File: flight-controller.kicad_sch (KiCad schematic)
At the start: 58 parts, among them J1 USB_C_Receptacle_USB2.0, Q1 NMOS, SW1 SW_Push, U1 AT32F435RGT7, U2 BMI270, U3 BMP280, U4 W25N01GVZEIG, U5 AT7456E, U6 TPS54302, U7 TPS54302, U8 TLV75733PDBV, U9 USBLC6-2P6

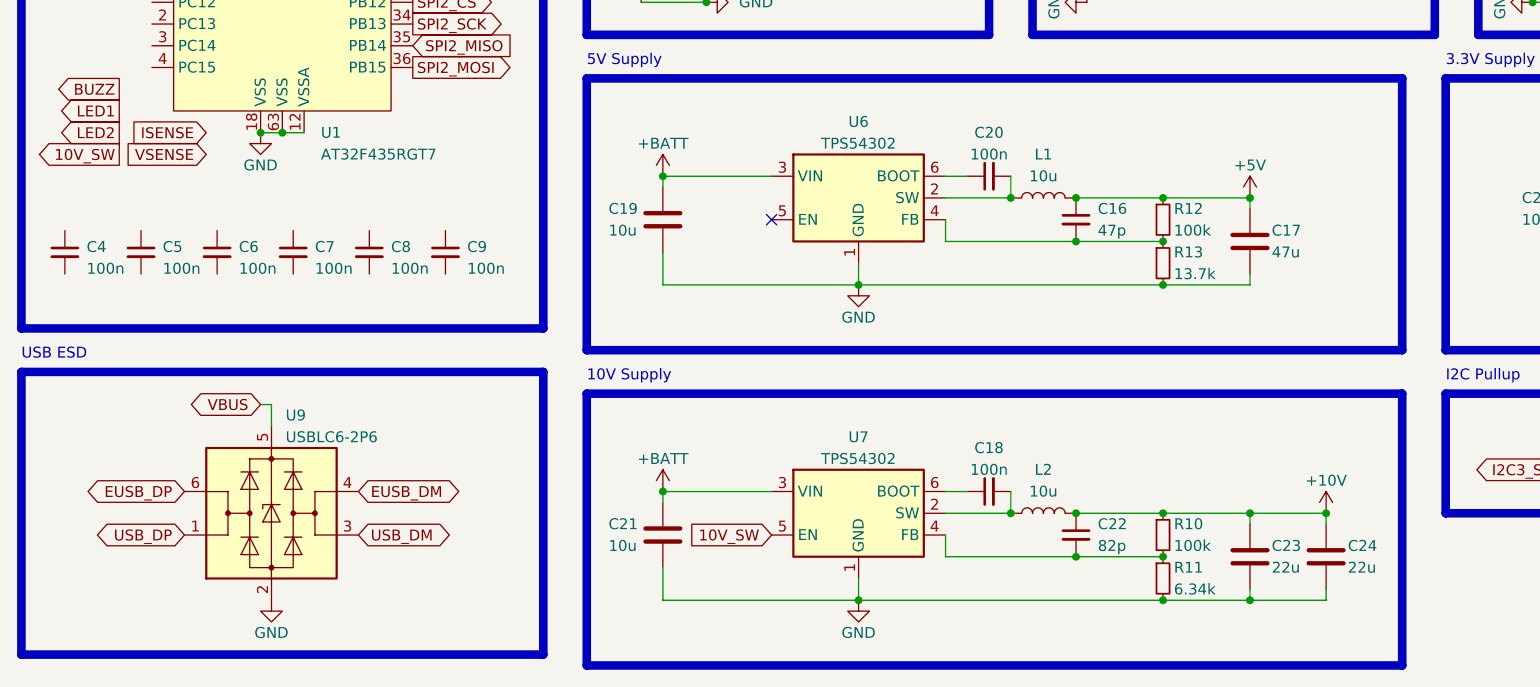
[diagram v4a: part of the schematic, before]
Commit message: Add LCSC part numbers for major parts. Provisionally delect power supply capacitors and inductors.
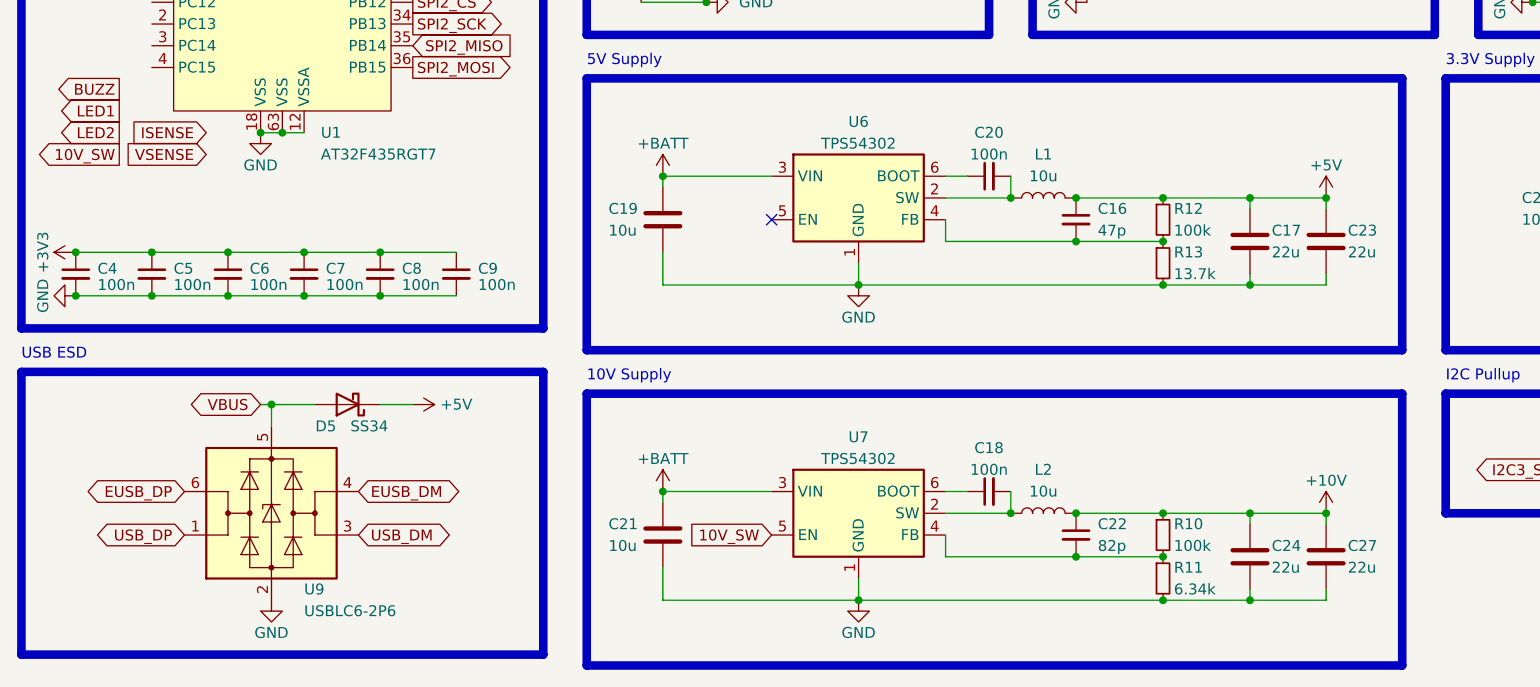
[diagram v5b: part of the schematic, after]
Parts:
- added C27: 22u, Capacitor_SMD:C_1206_3216Metric, symbol Device:C
- added D5: SS34, Diode_SMD:D_SMA, symbol Device:D_Schottky
- C17: value 47u -> 22u; footprint (none) -> Capacitor_SMD:C_1206_3216Metric; LCSC (none) -> C12891
- C23, C24: footprint (none) -> Capacitor_SMD:C_1206_3216Metric; LCSC (none) -> C12891
- J1: LCSC (none) -> C165948
- L1, L2: footprint (none) -> Inductor_SMD:L_Sunlord_MWSA0503S; LCSC (none) -> C408412
- U1: LCSC (none) -> C3029577
- U2: LCSC (none) -> C2836813
- U3: LCSC (none) -> C83291
- U4: LCSC (none) -> C88868
- U5: LCSC (none) -> C82351
- U6, U7: LCSC (none) -> C311983
- U8: LCSC (none) -> C485517
- U9: LCSC (none) -> C2827693
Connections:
- net +10V: now also C27.1; no longer C23.1
- net +3V3: now also C4.1, C5.1, C6.1, C7.1, C8.1, C9.1
- net +5V: now also C23.1, D5.1 (K)
- net GND: now also C4.2, C5.2, C6.2, C7.2, C8.2, C9.2, C27.2
- net VBUS: now also D5.2 (A)
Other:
- moved on the sheet: C4, C5, C6, C7, C8, C9

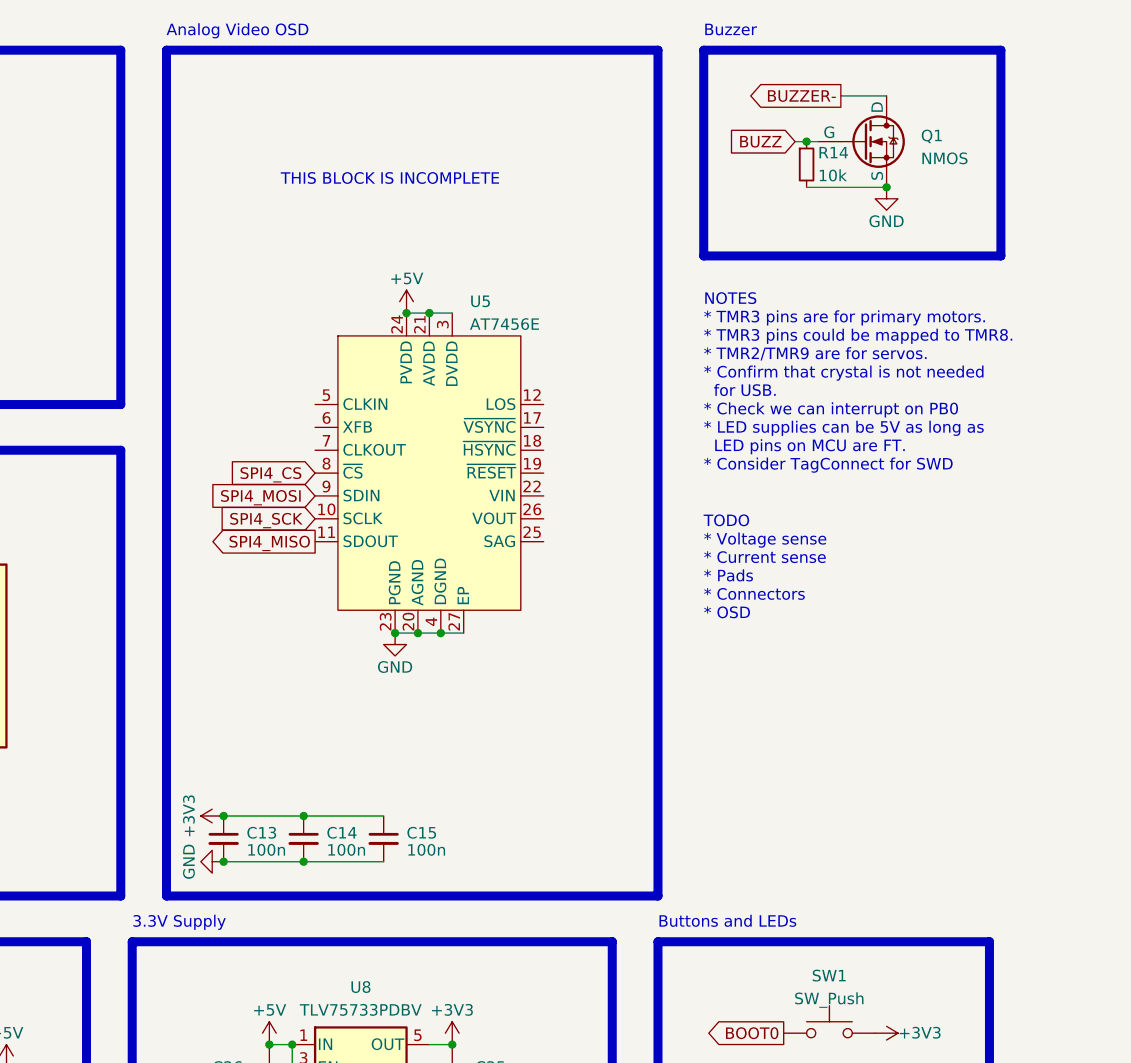
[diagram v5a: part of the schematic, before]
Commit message: Add remaining OSD components
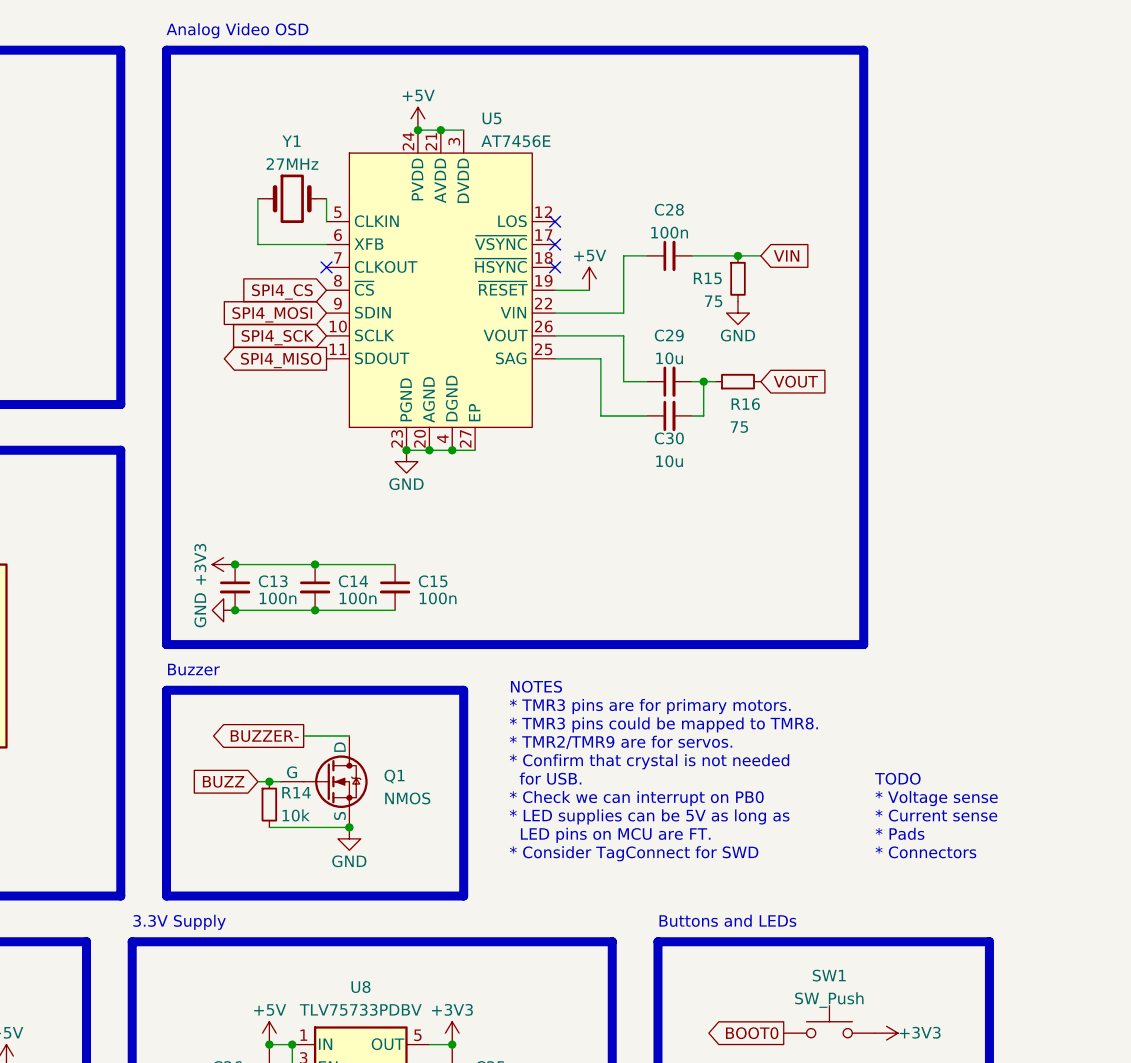
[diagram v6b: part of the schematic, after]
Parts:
- added C28: 100n, symbol Device:C_Small
- added C29, C30: 10u, symbol Device:C_Small
- added R15, R16: 75, symbol Device:R_Small
- added Y1: 27MHz, symbol Device:Crystal
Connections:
- net +5V: now also U5.19 (~{RESET})
- net GND: now also R15.2
- net at U5.22 (VIN): now also C28.1
- net at U5.25 (SAG): now also C30.1
- net at U5.26 (VOUT): now also C29.1
- net at U5.5 (CLKIN): now also Y1.2
- net at U5.6 (XFB): now also Y1.1
- new net: C29.2, C30.2, R16.1
- new net VIN: C28.2, R15.1
- new net VOUT: R16.2
- no-connect marks 8 -> 12
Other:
- note added: "TODO * Voltage sense * Current sense * Pads * Connectors"
- note removed: "THIS BLOCK IS INCOMPLETE"
- note removed: "TODO * Voltage sense * Current sense * Pads * Connectors * OSD"
- moved on the sheet: C13, C14, C15, Q1, R14, U5

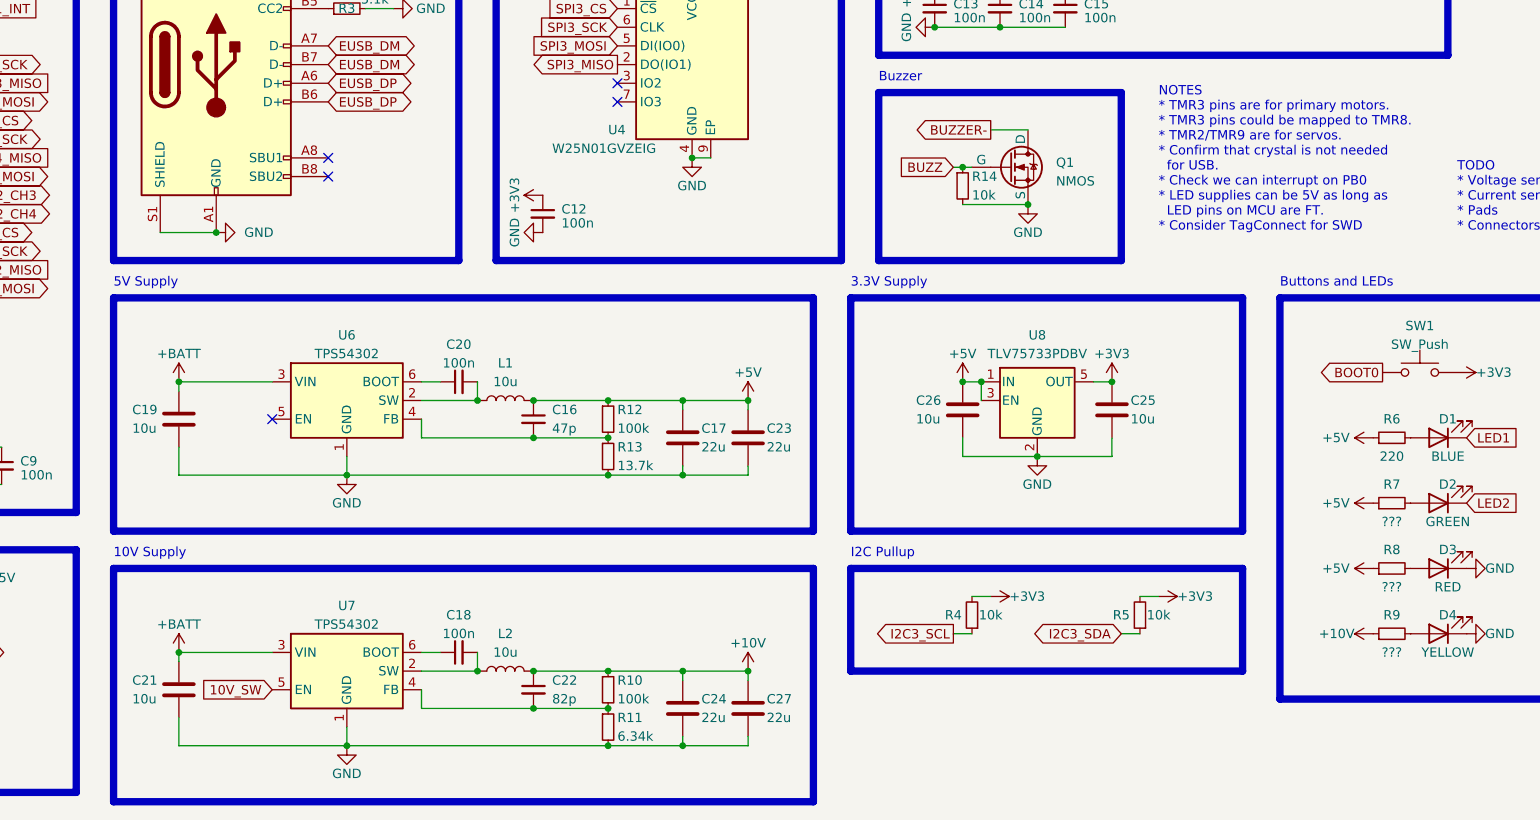
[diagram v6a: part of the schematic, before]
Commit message: Complete majority of component selection
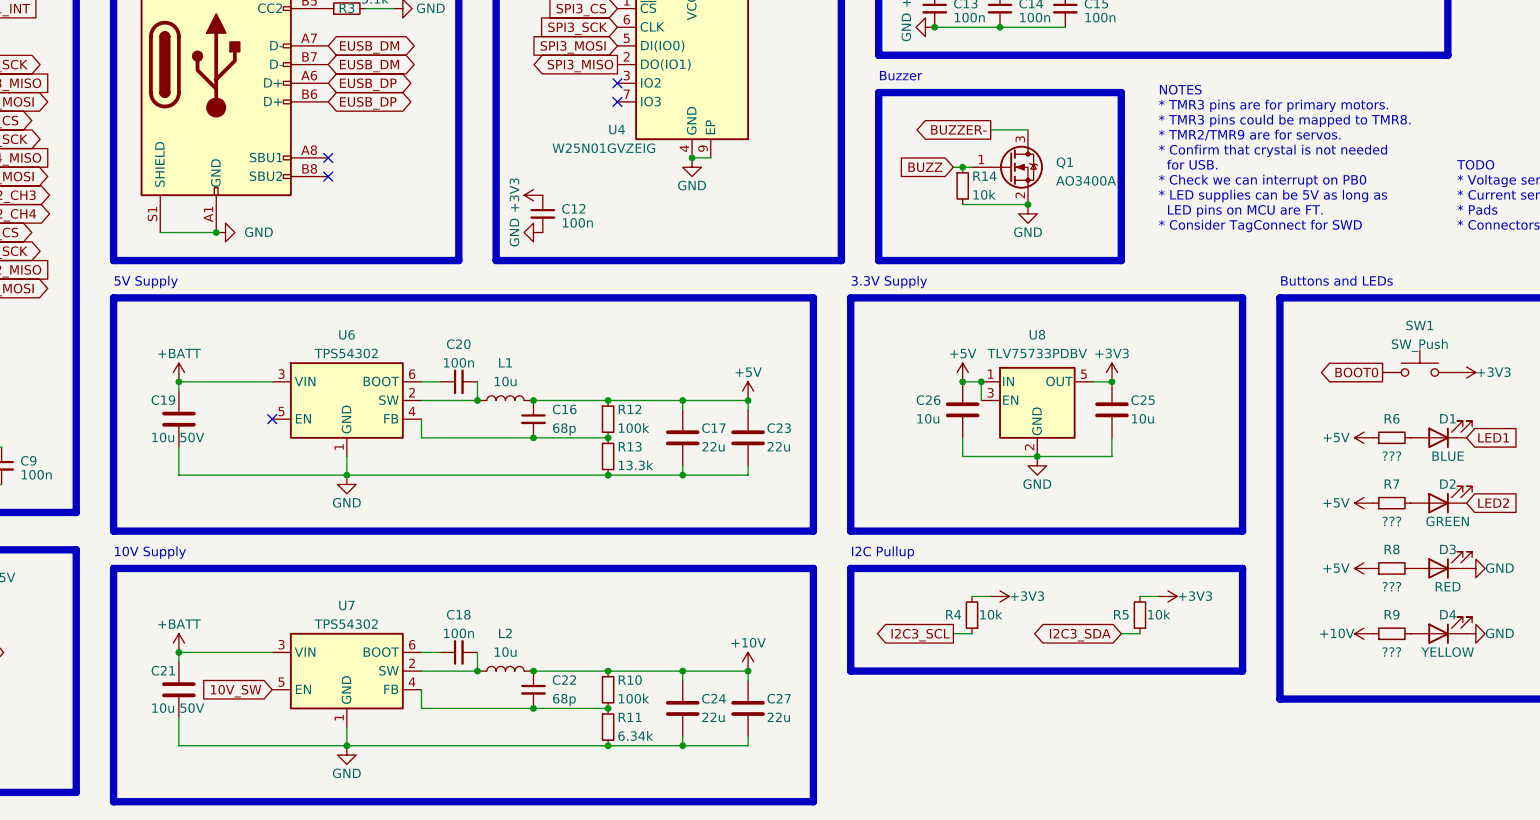
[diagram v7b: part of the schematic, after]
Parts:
- removed Q1: NMOS, symbol Simulation_SPICE:NMOS
- added Q1: AO3400A, Package_TO_SOT_SMD:SOT-23, symbol Transistor_FET:AO3400A
- C1, C10, C11, C12, C13, C14, C15, C18, C2, C20, C28, C3, C4, C5, C6, C7, C8, C9: footprint (none) -> Capacitor_SMD:C_0402_1005Metric; LCSC (none) -> C1525
- C16: value 47p -> 68p; footprint (none) -> Capacitor_SMD:C_0402_1005Metric; LCSC (none) -> C14441
- C19, C21: value 10u -> 10u 50V; footprint (none) -> Capacitor_SMD:C_1206_3216Metric; LCSC (none) -> C13585
- C22: value 82p -> 68p; footprint (none) -> Capacitor_SMD:C_0402_1005Metric; LCSC (none) -> C14441
- C25, C26, C29, C30: footprint (none) -> Capacitor_SMD:C_0603_1608Metric; LCSC (none) -> C19702
- D1: footprint (none) -> LED_SMD:LED_0603_1608Metric; LCSC (none) -> C72041
- D2: footprint (none) -> LED_SMD:LED_0603_1608Metric; LCSC (none) -> C72043
- D3: footprint (none) -> LED_SMD:LED_0603_1608Metric; LCSC (none) -> C181863
- D4: footprint (none) -> LED_SMD:LED_0603_1608Metric; LCSC (none) -> C72038
- R1, R14, R4, R5: footprint (none) -> Resistor_SMD:R_0402_1005Metric; LCSC (none) -> C25744
- R10, R12: footprint (none) -> Resistor_SMD:R_0402_1005Metric; LCSC (none) -> C25741
- R11: footprint (none) -> Resistor_SMD:R_0402_1005Metric; LCSC (none) -> C208926
- R13: value 13.7k -> 13.3k; footprint (none) -> Resistor_SMD:R_0402_1005Metric; LCSC (none) -> C310199
- R15, R16: footprint (none) -> Resistor_SMD:R_0402_1005Metric; LCSC (none) -> C25133
- R2, R3: footprint (none) -> Resistor_SMD:R_0402_1005Metric; LCSC (none) -> C25905
- R6: value 220 -> ???
- SW1: footprint (none) -> Button_Switch_SMD:SW_SPST_B3U-1000P; LCSC (none) -> C231329
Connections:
- net BUZZ: now also Q1.1 (G)
- net BUZZER-: now also Q1.3 (D)
- net GND: now also Q1.2 (S)
